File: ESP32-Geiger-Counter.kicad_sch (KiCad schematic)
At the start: 31 parts, among them J1 USB_C_Receptacle_USB2.0_16P, U1 TP4056-42-ESOP8, U2 USBLC6-2SC6, U3 ESP32-WROOM-32, U4 TPS63031DSK, U5 CP2102N-Axx-xQFN20

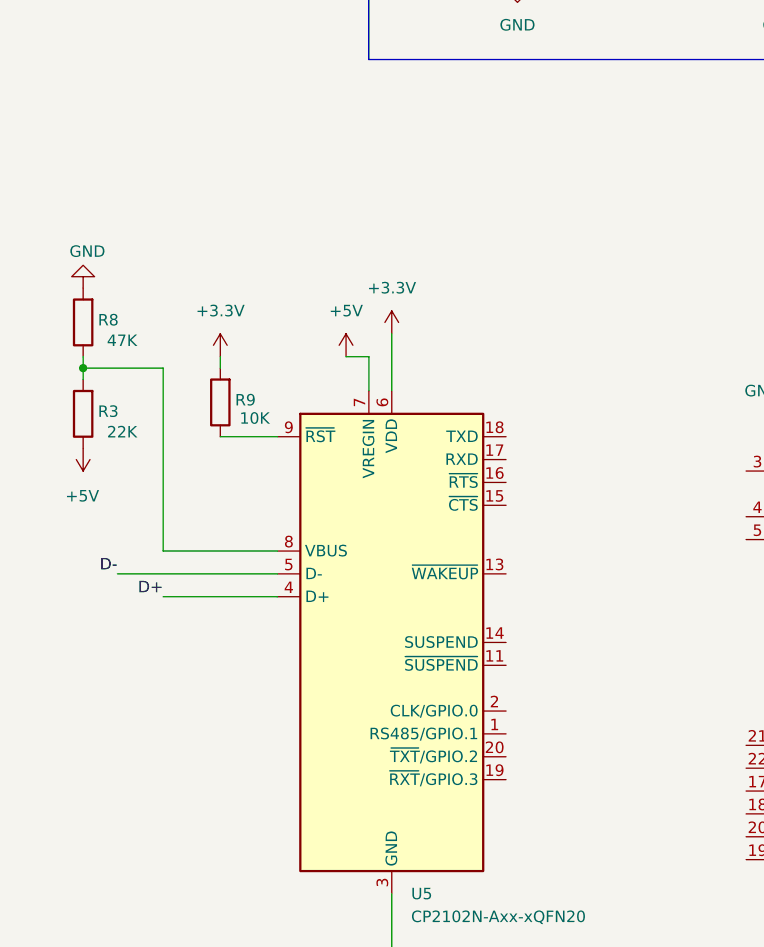
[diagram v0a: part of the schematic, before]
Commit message: working on usb protocol chip
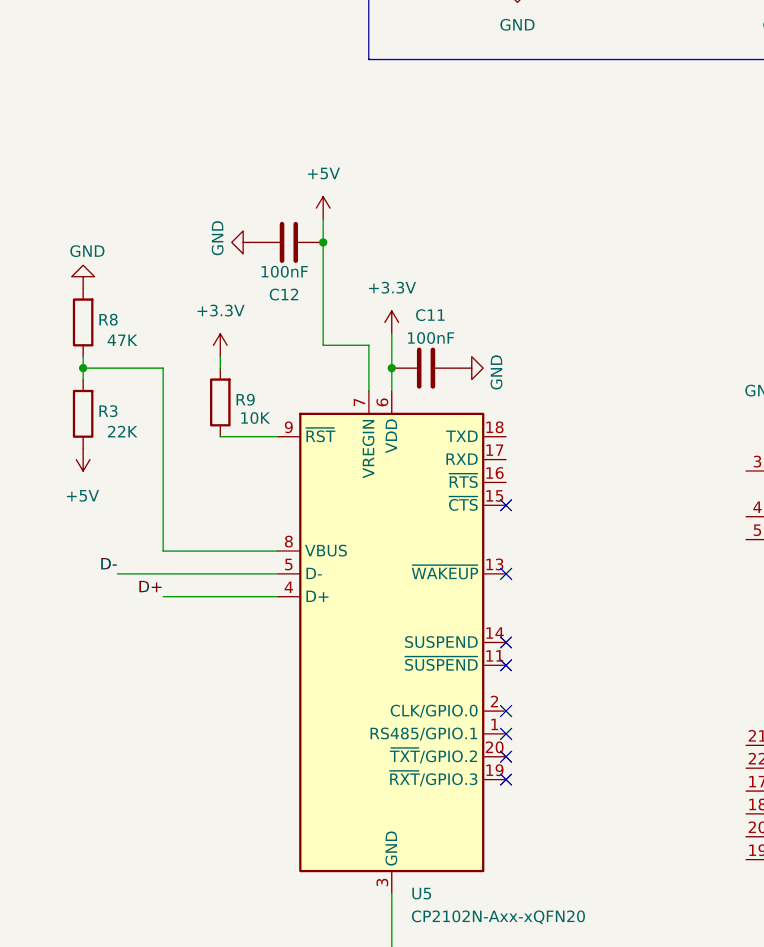
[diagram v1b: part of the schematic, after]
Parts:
- added C11, C12: 100nF, symbol Device:C
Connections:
- net +3.3V: now also C11.1
- net +5V: now also C12.1
- net GND: now also C11.2, C12.2
- no-connect marks 2 -> 10

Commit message: working on CP2102N
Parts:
- added C13: 10uF, symbol Device:C
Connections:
- net +5V: now also C13.2
- net RTS: now reaches U5.16 (~{RTS})
- net RXD: now reaches U5.17 (RXD)
- net TXD: now reaches U5.18 (TXD)
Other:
- moved on the sheet: C10, U3
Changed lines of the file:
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@@
 	)
 	(junction
-		(at 110.49 115.57)
+		(at 48.26 92.71)
+		(diameter 0)
+		(color 0 0 0 0)
+	)
+	(junction
+		(at 132.08 123.19)
 		(diameter 0)
 		(color 0 0 0 0)
@@
 	(wire
 		(pts
+			(xy 68.58 120.65) (xy 74.93 120.65)
+		)
+		(stroke
+			(width 0)
+			(type default)
+		)
+	)
+	(wire
+		(pts
 			(xy 92.71 35.56) (xy 85.09 35.56)
 		)
@@
 	(wire
 		(pts
-			(xy 110.49 111.76) (xy 110.49 115.57)
+			(xy 132.08 119.38) (xy 132.08 123.19)
 		)
 		(stroke
@@
 	(wire
 		(pts
-			(xy 48.26 96.52) (xy 48.26 99.06)
+			(xy 48.26 88.9) (xy 48.26 92.71)
 		)
 		(stroke
@@
 	(wire
 		(pts
+			(xy 48.26 92.71) (xy 48.26 99.06)
+		)
+		(stroke
+			(width 0)
+			(type default)
+		)
+	)
+	(wire
+		(pts
 			(xy 154.94 46.99) (xy 154.94 53.34)
 		)
@@
 	(wire
 		(pts
+			(xy 68.58 123.19) (xy 78.74 123.19)
+		)
+		(stroke
+			(width 0)
+			(type default)
+		)
+	)
+	(wire
+		(pts
 			(xy 104.14 63.5) (xy 104.14 64.77)
 		)
@@
 	(wire
 		(pts
-			(xy 110.49 190.5) (xy 110.49 195.58)
+			(xy 132.08 198.12) (xy 132.08 203.2)
 		)
 		(stroke
@@
 	(wire
 		(pts
-			(xy 110.49 115.57) (xy 110.49 119.38)
+			(xy 132.08 123.19) (xy 132.08 127)
 		)
 		(stroke
@@
 	(wire
 		(pts
+			(xy 68.58 125.73) (xy 82.55 125.73)
+		)
+		(stroke
+			(width 0)
+			(type default)
+		)
+	)
+	(wire
+		(pts
 			(xy 90.17 40.64) (xy 90.17 38.1)
 		)
@@
 		)
 	)
+	(label "RXD"
+		(at 78.74 123.19 0)
+		(effects
+			(font
+				(size 1.27 1.27)
+			)
+			(justify left bottom)
+		)
+	)
 	(label "VPWR"
 		(at 209.55 74.93 180)
@@
 		)
 	)
+	(label "RTS"
+		(at 82.55 125.73 0)
+		(effects
+			(font
+				(size 1.27 1.27)
+			)
+			(justify left bottom)
+		)
+	)
 	(label "VBAT"
 		(at 210.82 30.48 180)
@@
 		)
 	)
+	(label "TXD"
+		(at 74.93 120.65 0)
+		(effects
+			(font
+				(size 1.27 1.27)
+			)
+			(justify left bottom)
+		)
+	)
 	(label "D-"
 		(at 92.71 63.5 180)
@@
 	(symbol
 		(lib_id "power:+3.3V")
-		(at 110.49 111.76 0)
+		(at 132.08 119.38 0)
 		(unit 1)
 		(body_style 1)
@@
 		(fields_autoplaced yes)
 		(property "Reference" "#PWR021"
-			(at 110.49 115.57 0)
+			(at 132.08 123.19 0)
 			(hide yes)
 			(show_name no)
@@
 		)
 		(property "Value" "+3.3V"
-			(at 110.49 106.68 0)
+			(at 132.08 114.3 0)
 			(show_name no)
 			(do_not_autoplace no)
@@
 		)
 		(property "Footprint" ""
-			(at 110.49 111.76 0)
+			(at 132.08 119.38 0)
 			(hide yes)
 			(show_name no)
@@
 		)
 		(property "Datasheet" ""
-			(at 110.49 111.76 0)
+			(at 132.08 119.38 0)
 			(hide yes)
 			(show_name no)
@@
 		)
 		(property "Description" "Power symbol creates a global label with name \"+3.3V\""
-			(at 110.49 111.76 0)
+			(at 132.08 119.38 0)
 			(hide yes)
 			(show_name no)
@@
 	(symbol
 		(lib_id "power:GND")
-		(at 110.49 195.58 0)
+		(at 132.08 203.2 0)
 		(unit 1)
 		(body_style 1)
@@
 		(fields_autoplaced yes)
 		(property "Reference" "#PWR022"
-			(at 110.49 201.93 0)
+			(at 132.08 209.55 0)
 			(hide yes)
 			(show_name no)
@@
 		)
 		(property "Value" "GND"
-			(at 110.49 200.66 0)
+			(at 132.08 208.28 0)
 			(show_name no)
 			(do_not_autoplace no)
@@
 		)
 		(property "Footprint" ""
-			(at 110.49 195.58 0)
+			(at 132.08 203.2 0)
 			(hide yes)
 			(show_name no)
@@
 		)
 		(property "Datasheet" ""
-			(at 110.49 195.58 0)
+			(at 132.08 203.2 0)
 			(hide yes)
 			(show_name no)
@@
 		)
 		(property "Description" "Power symbol creates a global label with name \"GND\" , ground"
-			(at 110.49 195.58 0)
+			(at 132.08 203.2 0)
 			(hide yes)
 			(show_name no)
@@
 	(symbol
 		(lib_id "RF_Module:ESP32-WROOM-32")
-		(at 110.49 154.94 0)
+		(at 132.08 162.56 0)
 		(unit 1)
 		(body_style 1)
@@
 		(fields_autoplaced yes)
 		(property "Reference" "U3"
-			(at 112.6333 116.84 0)
+			(at 134.2233 124.46 0)
 			(show_name no)
 			(do_not_autoplace no)
@@
 		)
 		(property "Value" "ESP32-WROOM-32"
-			(at 112.6333 119.38 0)
+			(at 134.2233 127 0)
 			(show_name no)
 			(do_not_autoplace no)
@@
 		)
 		(property "Footprint" "RF_Module:ESP32-WROOM-32"
-			(at 110.49 193.04 0)
+			(at 132.08 200.66 0)
 			(hide yes)
 			(show_name no)
@@
 		)
 		(property "Datasheet" "https://www.espressif.com/sites/default/files/documentation/esp32-wroom-32_datasheet_en.pdf"
-			(at 102.87 153.67 0)
+			(at 124.46 161.29 0)
 			(hide yes)
 			(show_name no)
@@
 		)
 		(property "Description" "RF Module, ESP32-D0WDQ6 SoC, Wi-Fi 802.11b/g/n, Bluetooth, BLE, 32-bit, 2.7-3.6V, onboard antenna, SMD"
-			(at 110.49 154.94 0)
+			(at 132.08 162.56 0)
 			(hide yes)
 			(show_name no)
@@
 	(symbol
 		(lib_id "power:GND")
-		(at 102.87 115.57 270)
+		(at 124.46 123.19 270)
 		(unit 1)
 		(body_style 1)
@@
 		(fields_autoplaced yes)
 		(property "Reference" "#PWR023"
-			(at 96.52 115.57 0)
+			(at 118.11 123.19 0)
 			(hide yes)
 			(show_name no)
@@
 		)
 		(property "Value" "GND"
-			(at 99.06 115.5699 90)
+			(at 120.65 123.1899 90)
 			(show_name no)
 			(do_not_autoplace no)
@@
 		)
 		(property "Footprint" ""
-			(at 102.87 115.57 0)
+			(at 124.46 123.19 0)
 			(hide yes)
 			(show_name no)
@@
 		)
 		(property "Datasheet" ""
-			(at 102.87 115.57 0)
+			(at 124.46 123.19 0)
 			(hide yes)
 			(show_name no)
@@
 		)
 		(property "Description" "Power symbol creates a global label with name \"GND\" , ground"
-			(at 102.87 115.57 0)
+			(at 124.46 123.19 0)
 			(hide yes)
 			(show_name no)
@@
 	)
 	(symbol
+		(lib_id "Device:C")
+		(at 44.45 92.71 90)
+		(unit 1)
+		(body_style 1)
+		(exclude_from_sim no)
+		(in_bom yes)
+		(on_board yes)
+		(in_pos_files yes)
+		(dnp no)
+		(property "Reference" "C13"
+			(at 44.704 86.36 90)
+			(show_name no)
+			(do_not_autoplace no)
+			(effects
+				(font
+					(size 1.27 1.27)
+				)
+			)
+		)
+		(property "Value" "10uF"
+			(at 44.704 88.9 90)
+			(show_name no)
+			(do_not_autoplace no)
+			(effects
+				(font
+					(size 1.27 1.27)
+				)
+			)
+		)
+		(property "Footprint" ""
+			(at 48.26 91.7448 0)
+			(hide yes)
+			(show_name no)
+			(do_not_autoplace no)
+			(effects
+				(font
+					(size 1.27 1.27)
+				)
+			)
+		)
+		(property "Datasheet" ""
+			(at 44.45 92.71 0)
+			(hide yes)
+			(show_name no)
+			(do_not_autoplace no)
+			(effects
+				(font
+					(size 1.27 1.27)
+				)
+			)
+		)
+		(property "Description" "Unpolarized capacitor"
+			(at 44.45 92.71 0)
+			(hide yes)
+			(show_name no)
+			(do_not_autoplace no)
+			(effects
+				(font
+					(size 1.27 1.27)
+				)
+			)
+		)
+		(pin "2"
+		)
+		(pin "1"
+		)
+		(instances
+			(project "ESP32-Geiger-Counter"
+				(path "/1d04c1b6-b1c1-45fc-a2be-06365cafa415"
+					(reference "C13")
+					(unit 1)
+				)
+			)
+		)
+	)
+	(symbol
 		(lib_id "Device:R")
 		(at 140.97 69.85 90)
@@
 	(symbol
 		(lib_id "Device:C")
-		(at 106.68 115.57 90)
+		(at 128.27 123.19 90)
 		(unit 1)
 		(body_style 1)
@@
 		(dnp no)
 		(property "Reference" "C10"
-			(at 104.14 109.22 90)
+			(at 125.73 116.84 90)
 			(show_name no)
 			(do_not_autoplace no)
@@
 		)
 		(property "Value" "100nF"
-			(at 104.14 111.76 90)
+			(at 125.73 119.38 90)
 			(show_name no)
 			(do_not_autoplace no)
@@
 		)
 		(property "Footprint" ""
-			(at 110.49 114.6048 0)
+			(at 132.08 122.2248 0)
 			(hide yes)
 			(show_name no)
@@
 		)
 		(property "Datasheet" ""
-			(at 106.68 115.57 0)
+			(at 128.27 123.19 0)
 			(hide yes)
 			(show_name no)
@@
 		)
 		(property "Description" "Unpolarized capacitor"
-			(at 106.68 115.57 0)
+			(at 128.27 123.19 0)
 			(hide yes)
 			(show_name no)
@@
 	(symbol
 		(lib_id "power:+5V")
-		(at 48.26 96.52 0)
+		(at 48.26 88.9 0)
 		(unit 1)
 		(body_style 1)
@@
 		(fields_autoplaced yes)
 		(property "Reference" "#PWR028"
-			(at 48.26 100.33 0)
+			(at 48.26 92.71 0)
 			(hide yes)
 			(show_name no)
@@
 		)
 		(property "Value" "+5V"
-			(at 48.26 91.44 0)
+			(at 48.26 83.82 0)
 			(show_name no)
 			(do_not_autoplace no)
@@
 		)
 		(property "Footprint" ""
-			(at 48.26 96.52 0)
+			(at 48.26 88.9 0)
 			(hide yes)
 			(show_name no)
@@
 		)
 		(property "Datasheet" ""
-			(at 48.26 96.52 0)
+			(at 48.26 88.9 0)
 			(hide yes)
 			(show_name no)
@@
 		)
 		(property "Description" "Power symbol creates a global label with name \"+5V\""
-			(at 48.26 96.52 0)
+			(at 48.26 88.9 0)
 			(hide yes)
 			(show_name no)

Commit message: added auto reset
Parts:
- removed U5: CP2102N-Axx-xQFN20, Package_DFN_QFN:SiliconLabs_QFN-20-1EP_3x3mm_P0.5mm_EP1.8x1.8mm, symbol Interface_USB:CP2102N-Axx-xQFN20
- added Q1, Q2: Q_NPN_BCE, symbol Transistor_BJT:Q_NPN_BCE
- added R10, R11: 10K, symbol Device:R
- added U6: CP2102N-Axx-xQFN24, Package_DFN_QFN:QFN-24-1EP_4x4mm_P0.5mm_EP2.6x2.6mm, symbol Interface_USB:CP2102N-Axx-xQFN24
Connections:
- net +3.3V: now also U6.5 (VIO), U6.6 (VDD)
- net +5V: now also U6.7 (VREGIN)
- net D+: now also U6.3 (D+)
- net D-: now also U6.4 (D-)
- net GND: now also U6.2 (GND), U6.25 (GND)
- net RTS: now also Q1.3 (E), R11.2, U6.19 (~{RTS})
- net RXD: now also U3.34 (RXD0/IO3), U6.20 (RXD)
- net TXD: now also U3.35 (TXD0/IO1), U6.21 (TXD)
- net at R3.2, R8.1: now also U6.8 (VBUS)
- net at R9.1: now also U6.9 (~{RST})
- net IO0: now reaches U3.25 (IO0)
- net IO0: now also Q2.3 (E)
- net EN: now reaches U3.3 (EN)
- net EN: now also Q1.2 (C)
- new net: Q2.1 (B), R11.1
- new net: Q1.1 (B), R10.1
- new net DTR: Q2.2 (C), R10.2, U6.23 (~{DTR})
- no-connect marks 10 -> 12
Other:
- note added: "Auto Reset"
- note added: "USB to ESP"
- moved on the sheet: BT1, C10, C11, C12, C13, R3, R8, R9, U3

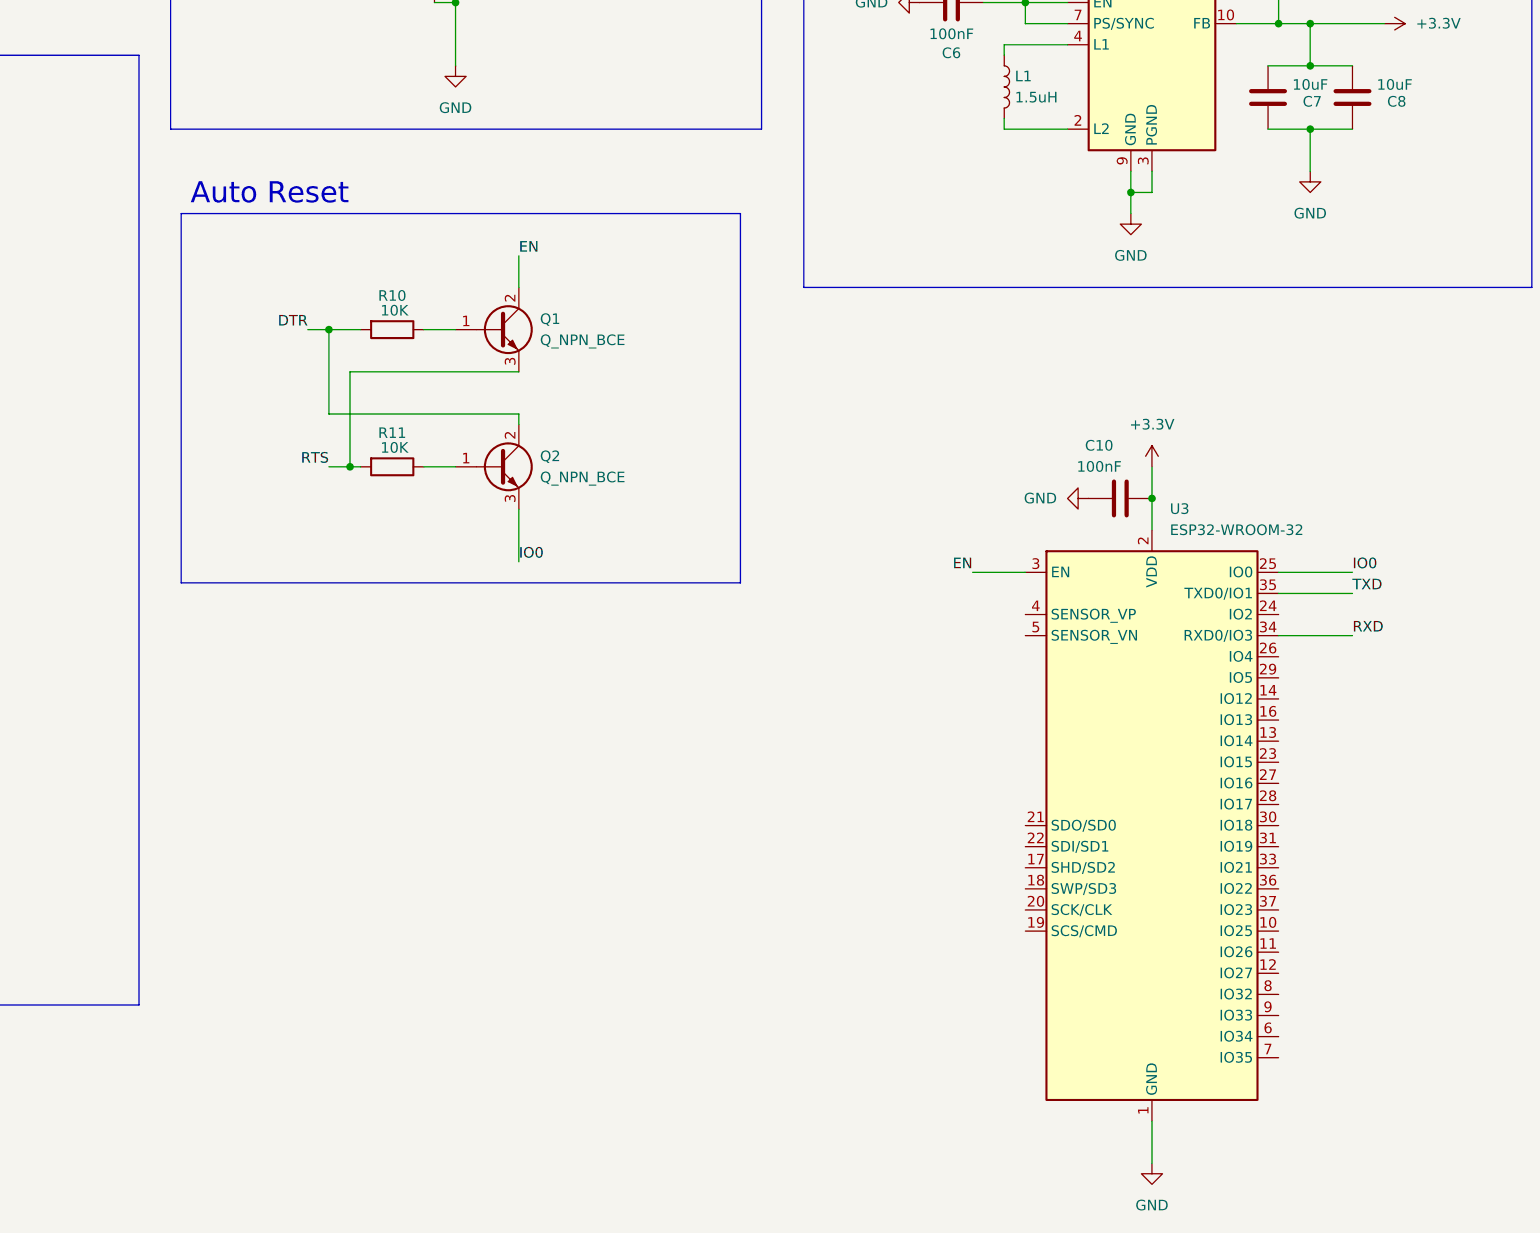
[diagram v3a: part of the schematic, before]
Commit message: boot and reset buttons
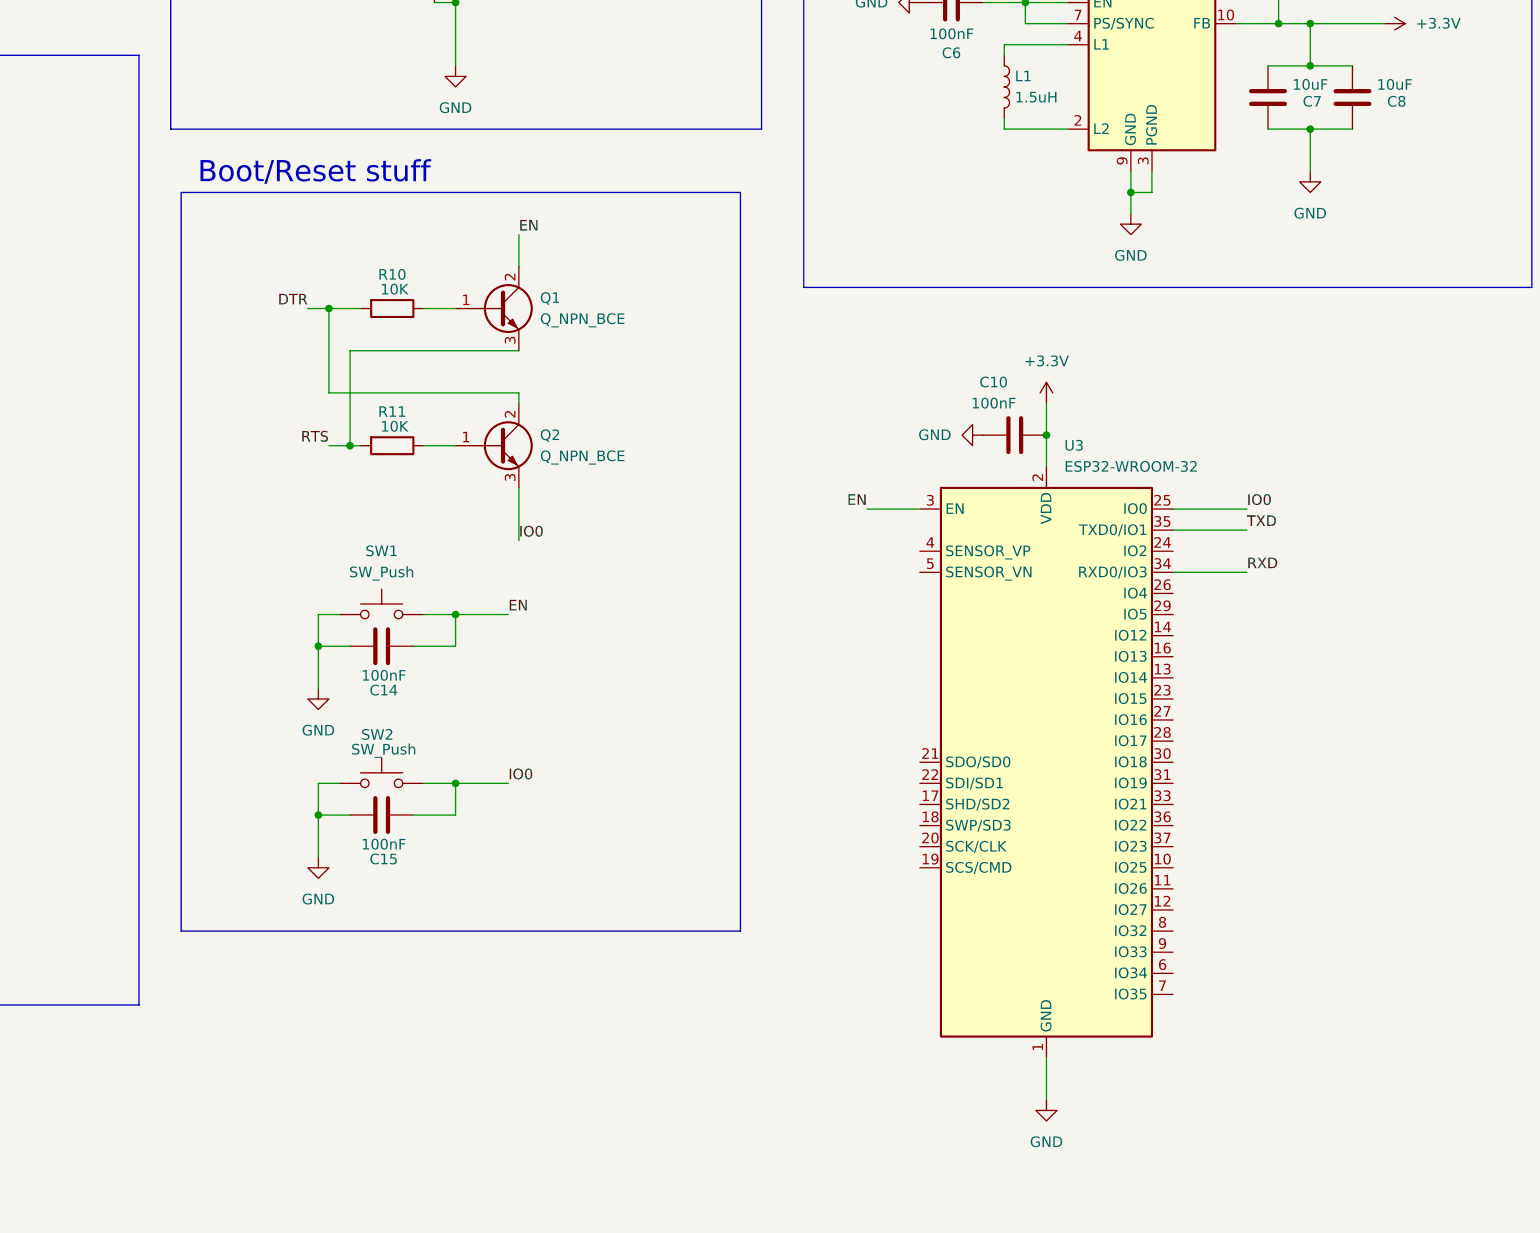
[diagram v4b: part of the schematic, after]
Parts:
- added C14, C15: 100nF, symbol Device:C
- added SW1, SW2: SW_Push, symbol Switch:SW_Push
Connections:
- net EN: now also C14.2, SW1.2
- net GND: now also C14.1, C15.1, SW1.1, SW2.1
- net IO0: now also C15.2, SW2.2
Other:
- note added: "Boot/Reset stuff"
- note removed: "Auto Reset"
- moved on the sheet: C10, Q1, Q2, R10, R11, U3
